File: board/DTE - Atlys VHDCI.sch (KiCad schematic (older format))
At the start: 3 parts, among them J201 DIGILENT_VHDCI_CONN

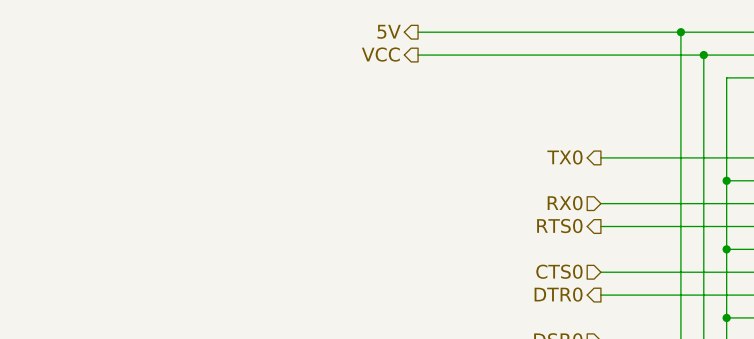
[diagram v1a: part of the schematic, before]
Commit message: Fixed power pin and port names to include voltages
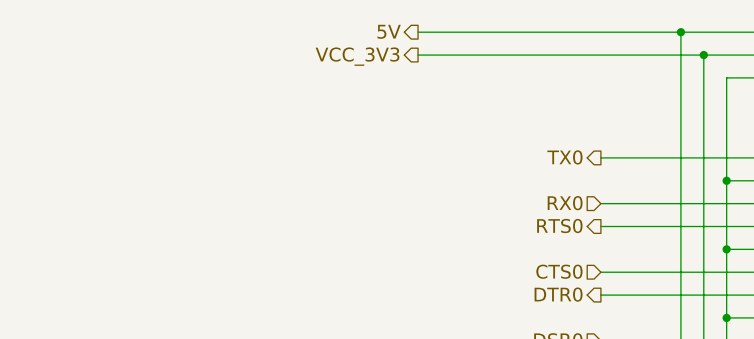
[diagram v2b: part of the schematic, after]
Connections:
- net VCC renamed VCC_3V3
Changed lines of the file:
@@
 5V
 Text HLabel 3650 1800 0    60   Output ~ 0
-VCC
+VCC_3V3
 Text HLabel 4450 4450 0    60   Output ~ 0
 TX2
